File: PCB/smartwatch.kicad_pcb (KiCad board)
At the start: 2 copper layers, 37 x 23.5 mm, 55 parts, among them U1 STM32F103C8T6, U2 HM-10, U3 M25P40, U4 BMC150, U5 BMP180, U6 STC4054, U7 NCP551, U8 UG-2864HSWEG01, X1 PLS1, X2 PLS1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

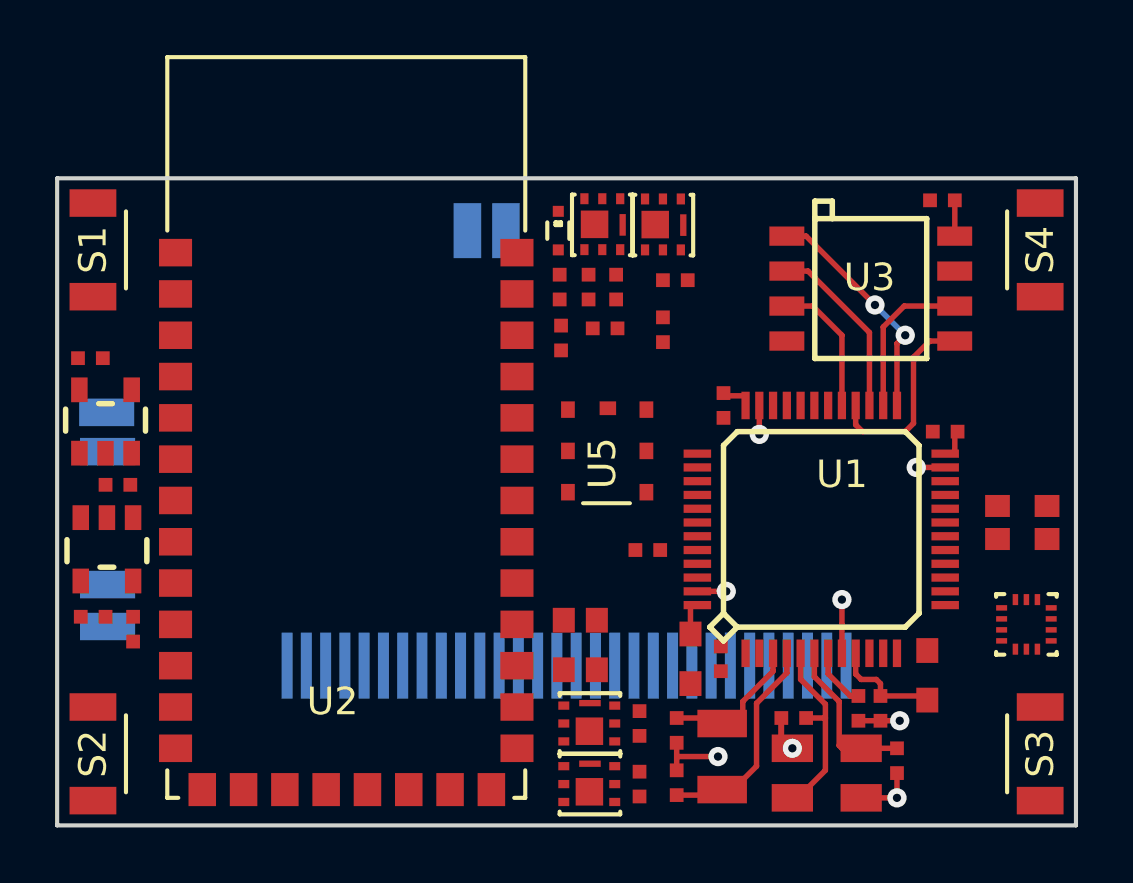
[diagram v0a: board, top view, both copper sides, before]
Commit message: First iteration (only SH1106 and some GUI classes work fine)
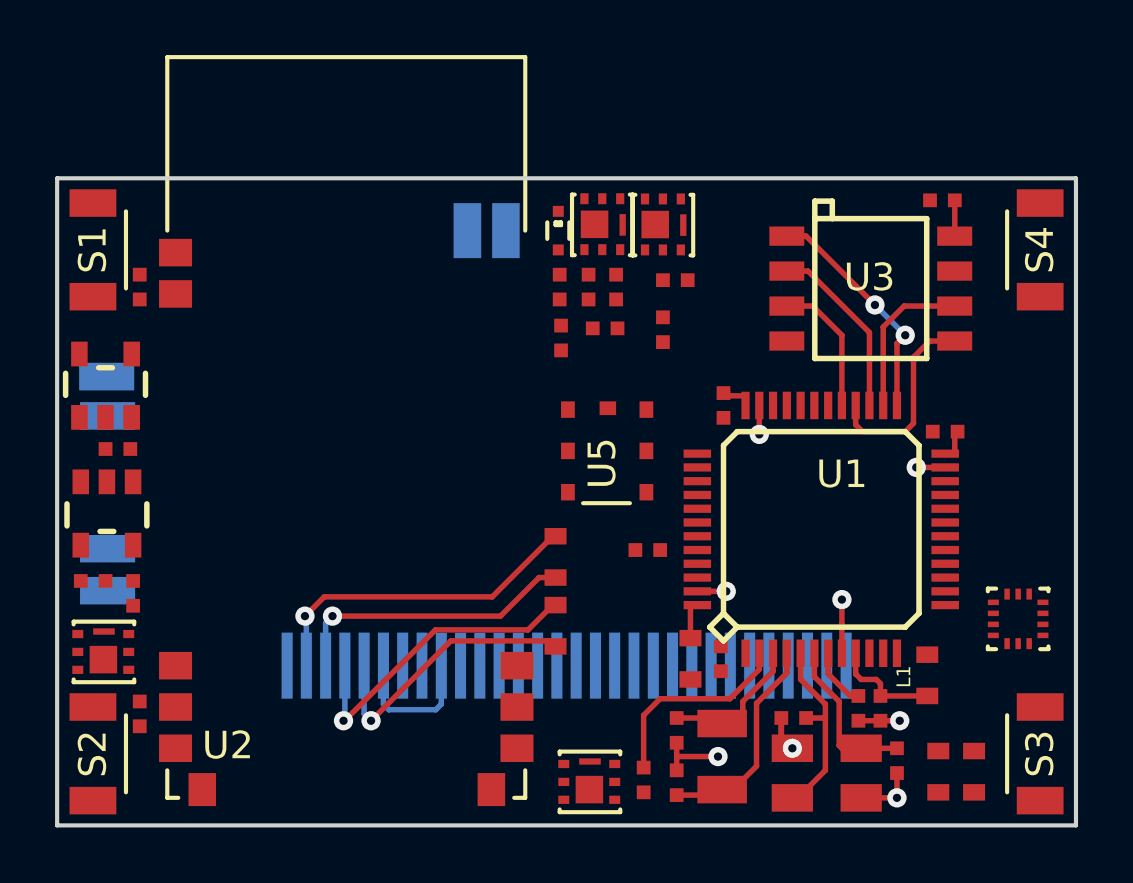
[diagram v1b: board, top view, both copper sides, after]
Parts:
- C15, C16, C17, C18: value capacitor -> 1u/10V
- R11: value resistor -> 390k
- U2: value HM-10 -> HM-10_MIN; footprint MODULES:HM-10 -> MODULES:HM-10_MIN
- moved R7 18.3 mm to (177.0, 100.4)
- moved VT2 18.3 mm to (176.7, 98.7)
- moved C18 8.96 mm to (207.3, 101.3), turned to 270 degrees
- moved C17 8.04 mm to (206.0, 101.3), turned to 270 degrees
- moved C7 3.32 mm to (177.0, 84.0), turned to 270 degrees
- moved C15 2.27 mm to (192.1, 95.0), turned to 90 degrees
- moved VT1 2.12 mm to (194.3, 103.4)
- moved R6 2.06 mm to (195.3, 101.9)
- moved C6 1.30 mm to (176.7, 90.3)
- moved C8 1.30 mm to (175.8, 95.1)
- moved X1 1.30 mm to (175.8, 94.0)
- moved X2 1.30 mm to (175.8, 95.5)
- moved R1 1.30 mm to (176.8, 96.0)
- moved U6 1.30 mm to (176.8, 91.5)
- moved U7 1.30 mm to (174.8, 89.2)
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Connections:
- U1 pad 1: Net-(U1-Pad1) -> /3V3
- U1 pad 2: Net-(U1-Pad2) -> /DISP_EN
- U1 pad 41: Net-(U1-Pad41) -> /DISP_nCS
- U1 pad 42: Net-(U1-Pad42) -> /DISP_nRES
- U1 pad 43: Net-(U1-Pad43) -> /DISP_DC
- U1 pad 45: Net-(U1-Pad45) -> /DISP_CLK
- U1 pad 46: Net-(U1-Pad46) -> /DISP_MOSI
- U8 pad 13: Net-(U8-Pad13) -> /DISP_nCS
- U8 pad 14: Net-(U8-Pad14) -> /DISP_nRES
- U8 pad 15: Net-(U8-Pad15) -> /DISP_DC
- U8 pad 18: Net-(U8-Pad18) -> /DISP_CLK
- U8 pad 19: Net-(U8-Pad19) -> /DISP_MOSI
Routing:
- net Net-(C15-Pad2): track 0.00 -> 12.1 mm, vias 0 -> 1
- net Net-(C16-Pad2): track 0.00 -> 11.5 mm, vias 0 -> 1
- net Net-(C15-Pad1): track 0.00 -> 10.6 mm, vias 0 -> 1
- net Net-(C16-Pad1): track 0.00 -> 10.1 mm, vias 0 -> 1
- net /DISP_EN: track 0.00 -> 7.37 mm
- net /DISP_PWR: track 0.00 -> 5.07 mm

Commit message: SPI Flash nWR is connected to 3V3
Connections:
- U1 pad 29: /MEM_WP -> Net-(U1-Pad29)
- U3 pad 3: /MEM_WP -> /3V3
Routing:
- net /MEM_WP: track 4.99 -> 0.00 mm

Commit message: PCB (everything is done, should be checked)
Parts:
- added C20: capacitor, discrete_SMD:0402_C, F.Cu at (208.6, 94.6)
- added LG?1: LOGO, LOGO:OSHW, F.Cu at (194.1, 87.5)
- added R12: resistor, discrete_SMD:0402_R, F.Cu at (208.2, 86.6)
- added R13: resistor, discrete_SMD:0402_R, F.Cu at (208.2, 84.8)
- added R14: 390k, discrete_SMD:0402_R, F.Cu at (192.8, 85.2)
- added R15: 390k, discrete_SMD:0402_R, F.Cu at (192.8, 84.3)
- added VT5: MOSFET_P_DGS, IR:PQFN2x2, F.Cu at (174.7, 92.7)
- added X10: 3V3, CONNECTORS:SLD_POINT, B.Cu at (200.7, 91.3)
- added X7: SWCLK, CONNECTORS:SLD_POINT, B.Cu at (200.7, 94.1)
- added X8: SWDIO, CONNECTORS:SLD_POINT, B.Cu at (200.7, 89.9)
- added X9: GND, CONNECTORS:SLD_POINT, B.Cu at (200.7, 92.7)
- U8: value UG-2864HSWEG01 -> SH1106
- X1: value PLS1 -> VCHRG
- X2, X4: value PLS1 -> GND
- X3, X5: value PLS1 -> VBAT
- X6: value PLS1 -> VMOT
- moved U7 25.0 mm to (198.9, 82.5), turned to 180 degrees
- moved C7 21.1 mm to (198.0, 85.9), turned to 0 degrees
- moved C6 20.4 mm to (196.0, 83.7), turned to 90 degrees
- moved R5 20.2 mm to (177.3, 91.7), turned to 270 degrees
- moved R7 19.5 mm to (194.6, 92.0), turned to 180 degrees
- moved R9 18.8 mm to (174.9, 88.9)
- moved R4 18.7 mm to (177.3, 87.1)
- moved VT4 18.5 mm to (176.7, 86.1), turned to 180 degrees
- moved C5 18.1 mm to (174.9, 89.8), turned to 0 degrees
- moved VT2 16.0 mm to (191.4, 92.2), turned to 0 degrees
- moved R8 15.8 mm to (176.7, 88.9), turned to 270 degrees
- moved X4 15.4 mm to (175.5, 103.1)
- moved U5 13.9 mm to (206.2, 87.3)
- moved X3 9.78 mm to (175.5, 98.9)
- moved R11 9.35 mm to (206.5, 101.6)
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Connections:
- net /BT_RST renamed Net-(U2-Pad11)
- net Net-(C9-Pad2) renamed /VDDA
- C5 pad 1: /VBAT_ADC -> GND
- C5 pad 2: GND -> /VBAT_ADC
- R5 pad 1: Net-(R4-Pad2) -> /VBAT
- R5 pad 2: GND -> Net-(R5-Pad2)
- R8 pad 1: /VBAT -> /VBAT_ADC
- R8 pad 2: /VBAT_ADC -> Net-(R8-Pad2)
- R9 pad 1: /VBAT_ADC -> GND
- R9 pad 2: Net-(R9-Pad2) -> /VBAT_ADC
- S1 pad 1: Net-(S1-Pad1) -> /S1
- S1 pad 2: Net-(S1-Pad2) -> GND
- S2 pad 1: Net-(S2-Pad1) -> GND
- S2 pad 2: Net-(S2-Pad2) -> /S2
- S3 pad 1: Net-(S3-Pad1) -> /S3
- S3 pad 2: Net-(S3-Pad2) -> GND
- S4 pad 1: Net-(S4-Pad1) -> GND
- S4 pad 2: Net-(S4-Pad2) -> /S4
- U1 pad 10: Net-(U1-Pad10) -> /VBAT_ADC
- U1 pad 11: Net-(U1-Pad11) -> /S3
- U1 pad 12: Net-(U1-Pad12) -> /VBAT_EN
- U1 pad 13: Net-(U1-Pad13) -> /BT_STATE
- U1 pad 16: Net-(U1-Pad16) -> /S4
- U1 pad 17: Net-(U1-Pad17) -> /ACC_IRQ3
- U1 pad 18: Net-(U1-Pad18) -> /ACC_DRDY
- U1 pad 19: Net-(U1-Pad19) -> /ACC_IRQ2
- U1 pad 20: Net-(U1-Pad20) -> /ACC_IRQ1
- U1 pad 21: Net-(U1-Pad21) -> /I2C_SCL
- U1 pad 22: Net-(U1-Pad22) -> /I2C_SDA
- U1 pad 29: Net-(U1-Pad29) -> /MOT_EN
- U1 pad 30: Net-(U1-Pad30) -> /BT_TX
- U1 pad 31: Net-(U1-Pad31) -> /BT_RX
- U1 pad 33: Net-(U1-Pad33) -> /S1
- U1 pad 34: Net-(U1-Pad34) -> /SWDIO
- U1 pad 37: Net-(U1-Pad37) -> /SWCLK
- U1 pad 38: Net-(U1-Pad38) -> /CHRG
- U1 pad 39: Net-(U1-Pad39) -> /S2
- U1 pad 40: Net-(U1-Pad40) -> /BT_EN
- U2 pad 24: Net-(U2-Pad24) -> /BT_STATE
- U4 pad 1: Net-(U4-Pad1) -> GND
- U4 pad 10: Net-(U4-Pad10) -> /3V3
- U4 pad 11: Net-(U4-Pad11) -> /I2C_SCL
- U4 pad 12: Net-(U4-Pad12) -> /3V3
- U4 pad 13: Net-(U4-Pad13) -> /3V3
- U4 pad 14: Net-(U4-Pad14) -> /I2C_SDA
- U4 pad 2: Net-(U4-Pad2) -> /ACC_IRQ1
- U4 pad 3: Net-(U4-Pad3) -> /ACC_IRQ2
- U4 pad 4: Net-(U4-Pad4) -> /ACC_DRDY
- U4 pad 5: Net-(U4-Pad5) -> /ACC_IRQ3
- U4 pad 6: Net-(U4-Pad6) -> GND
- U4 pad 7: Net-(U4-Pad7) -> GND
- U4 pad 8: Net-(U4-Pad8) -> /3V3
- U4 pad 9: Net-(U4-Pad9) -> GND
- U5 pad 2: Net-(U5-Pad2) -> /3V3
- U5 pad 3: Net-(U5-Pad3) -> /3V3
- U5 pad 5: Net-(U5-Pad5) -> /I2C_SCL
- U5 pad 6: Net-(U5-Pad6) -> /I2C_SDA
- U5 pad 7: Net-(U5-Pad7) -> GND
- VT4 pad 1: Net-(R9-Pad2) -> Net-(R5-Pad2)
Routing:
- net GND: track 14.1 -> 221.7 mm, vias 8 -> 26
- net /3V3: track 4.93 -> 84.6 mm, vias 0 -> 3
- net /VBAT: track 0.00 -> 52.7 mm, vias 0 -> 6
- net /VBAT_ADC: track 0.00 -> 41.2 mm, vias 0 -> 4
- net /VBAT_EN: track 0.00 -> 36.6 mm, vias 0 -> 2
- net /BT_STATE: track 0.00 -> 30.5 mm, vias 0 -> 2
- net /S2: track 0.00 -> 29.5 mm, vias 0 -> 4
- net /S1: track 0.00 -> 26.2 mm
- net /BT_PWR: track 0.00 -> 21.9 mm
- net /CHRG: track 0.00 -> 21.3 mm, vias 0 -> 2
- net Net-(R15-Pad2): track 0.00 -> 19.2 mm
- net /S4: track 0.00 -> 16.8 mm
- net /I2C_SCL: track 0.00 -> 15.2 mm, vias 0 -> 2
- net Net-(R14-Pad2): track 0.00 -> 14.4 mm
- net /DISP_PWR: track 5.07 -> 19.2 mm, vias 0 -> 3
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- added copper zone on F.Cu, net /3V3
- added copper zone on B.Cu, net GND
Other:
- net class ACC added: clearance 0.18, trace_width 0.16, via_dia 0.7, via_drill 0.3
- net class PWR added: clearance 0.3, trace_width 0.3, via_dia 0.7, via_drill 0.3
- rule trace_min: 0.2 -> 0.16

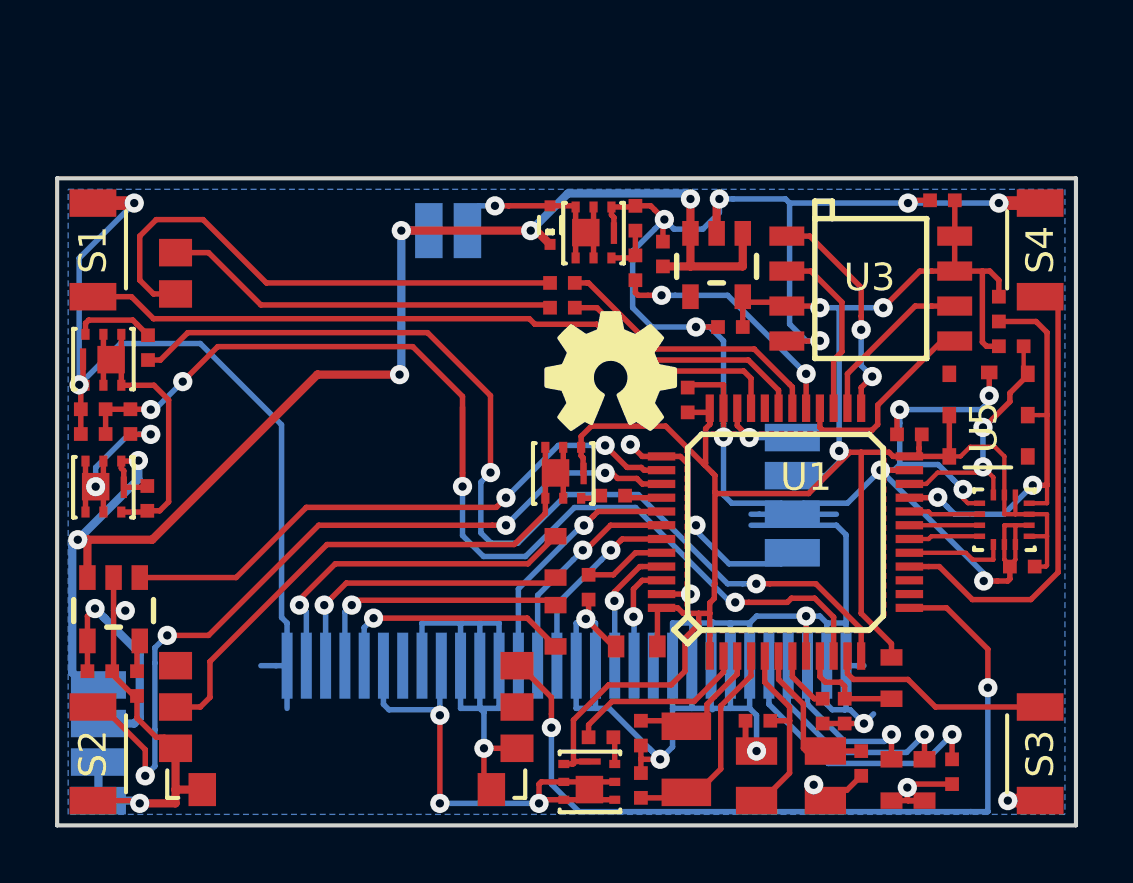
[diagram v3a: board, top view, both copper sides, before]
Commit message: PCB: Preparing production files
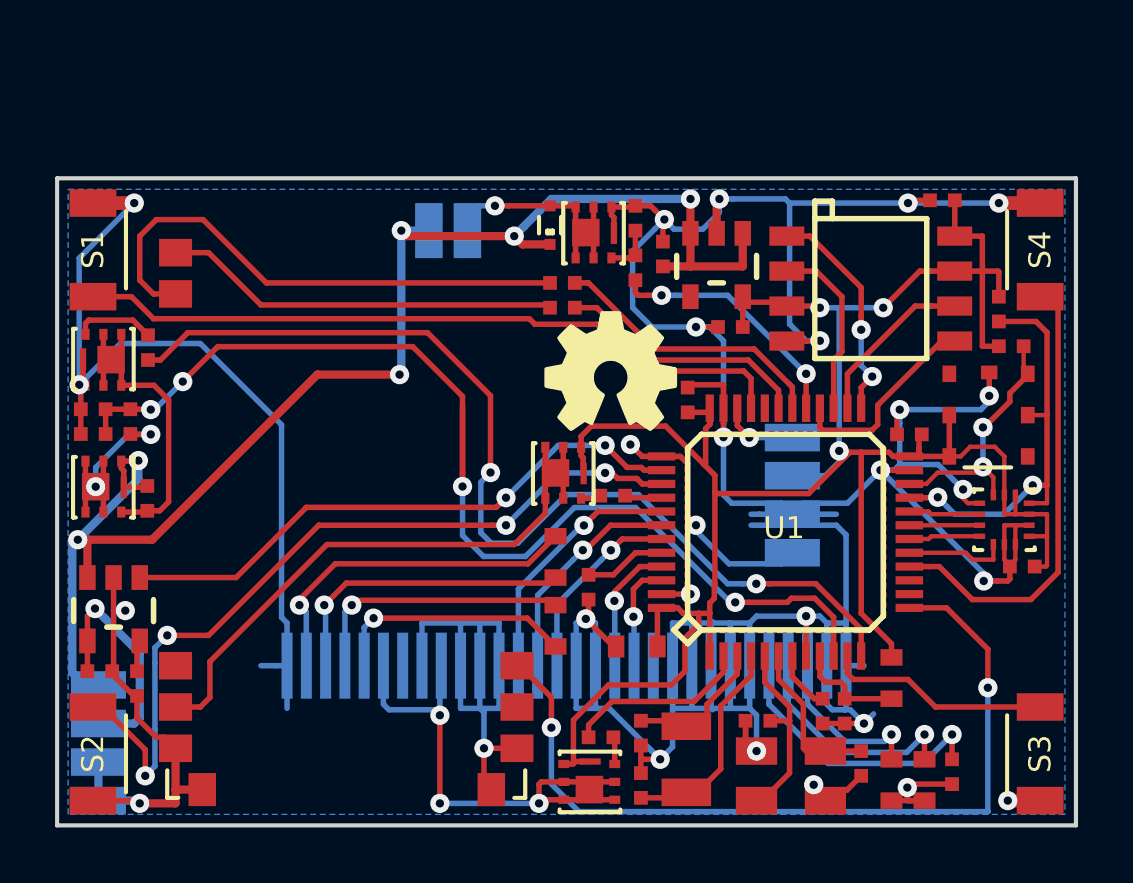
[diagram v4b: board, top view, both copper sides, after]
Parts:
- X1: value VCHRG -> VIN
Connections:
- net /VCHRG renamed /VIN
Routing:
- net /3V3: track 84.6 -> 85.9 mm
- net /VBAT: track 52.7 -> 53.2 mm
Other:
- board text added: "- +"
- board text added: "GND"
- board text added: "MOT"
- board text added: "SWCLK"
- board text added: "SWDIO"
- board text added: "SmartWatch"
- board text added: "VBAT"
- board text added: "VCC"
- board text added: "VIN"
- board text added: "www.sl-alex.com.ua"
